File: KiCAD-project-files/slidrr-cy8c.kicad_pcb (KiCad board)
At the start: 2 copper layers, 500 x 136.5 mm, 118 parts, among them J1 ISSP U1, J2 ISSP U2, J3 Conn_01x32_Socket, J4 JST-XH Series, J5 JST-XH Series, SW1 SW_DIP_x04, SW2 SW_Push, SW3 SW_Push, U5 SN74LV1T34DBVR

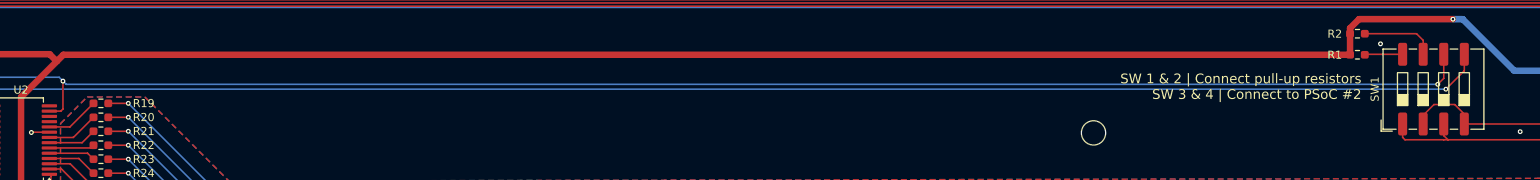
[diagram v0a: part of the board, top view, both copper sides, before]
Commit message: Edited PCB to fix floating UART issue. Added crappy WebUI for diagnosis
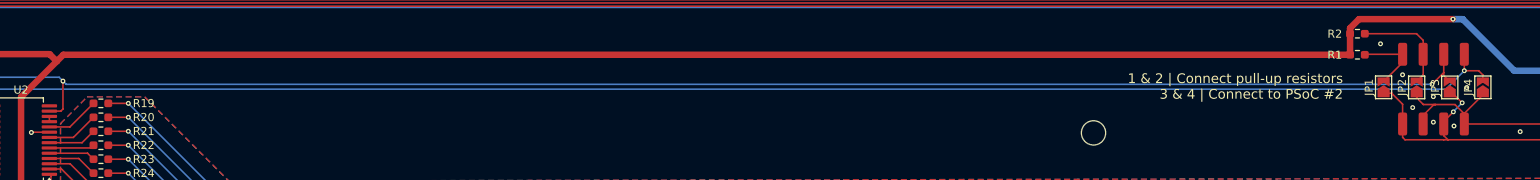
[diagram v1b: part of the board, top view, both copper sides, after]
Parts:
- added JP1: SW1, Jumper:SolderJumper-2_P1.3mm_Open_TrianglePad1.0x1.5mm, F.Cu at (330.8, 142.6)
- added JP2: SW2, Jumper:SolderJumper-2_P1.3mm_Open_TrianglePad1.0x1.5mm, F.Cu at (334.9, 142.6)
- added JP3: SW3, Jumper:SolderJumper-2_P1.3mm_Open_TrianglePad1.0x1.5mm, F.Cu at (339.0, 142.6)
- added JP4: SW4, Jumper:SolderJumper-2_P1.3mm_Open_TrianglePad1.0x1.5mm, F.Cu at (343.1, 142.6)
- C1, C3: value 4.7nF X7R -> 4.7nF X7R / 2.2nF X7R
- R10, R11, R12, R13, R14, R15, R16, R17, R18, R19, R20, R21, R22, R23, R24, R25, R26, R27, R28, R29, R3, R30, R31, R32, R33, R34, R4, R5, R6, R7, R8, R9: value R_Small -> 560R
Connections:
- C3 pad 2: Net-(U2-P0[7]) -> unconnected-(C3-Pad2)
- U2 pad 1: Net-(U2-P0[7]) -> unconnected-(U2-P0[7]-Pad1)
- U2 pad 11: UART_TX_U2 -> U2_UART_BRIDGE
- U2 pad 12: UART_RX_U2 -> U2_UART_BRIDGE
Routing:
- net I2C_SCL_U1: track 101.1 -> 112.9 mm, vias 2 -> 4
- net I2C_SDA_U1: track 86.8 -> 94.8 mm
- net Net-(R1-Pad1): track 4.68 -> 9.01 mm
- net Net-(R2-Pad1): track 9.27 -> 13.0 mm
- net I2C_SDA_U2: track 206.8 -> 210.1 mm
- net Net-(U2-P0[7]): track 2.14 -> 0.00 mm
- net (no net): track 0.00 -> 2.14 mm
- net I2C_SCL_U2: track 205.0 -> 206.0 mm
- net U2_UART_BRIDGE: track 0.00 -> 0.65 mm
- net GND: vias 54 -> 60
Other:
- board text added: "1 & 2 | Connect pull-up resistors 3 & 4 | Connect to PSoC #2"
- board text removed: "SW 1 & 2 | Connect pull-up resistors SW 3 & 4 | Connect to PSoC #2"
